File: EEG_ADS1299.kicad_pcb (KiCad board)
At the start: 2 copper layers, 45.2 x 21.7 mm, 70 parts, among them IC1 ADS1299, P1 CONN_2, P2 CONN_2, P3 CONN_1, P4 CONN_1, P5 CONN_01X08, U1 TPS61221, U2 TPS61222, U3 NRF528XX-QFAA, U4 MPU-9250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

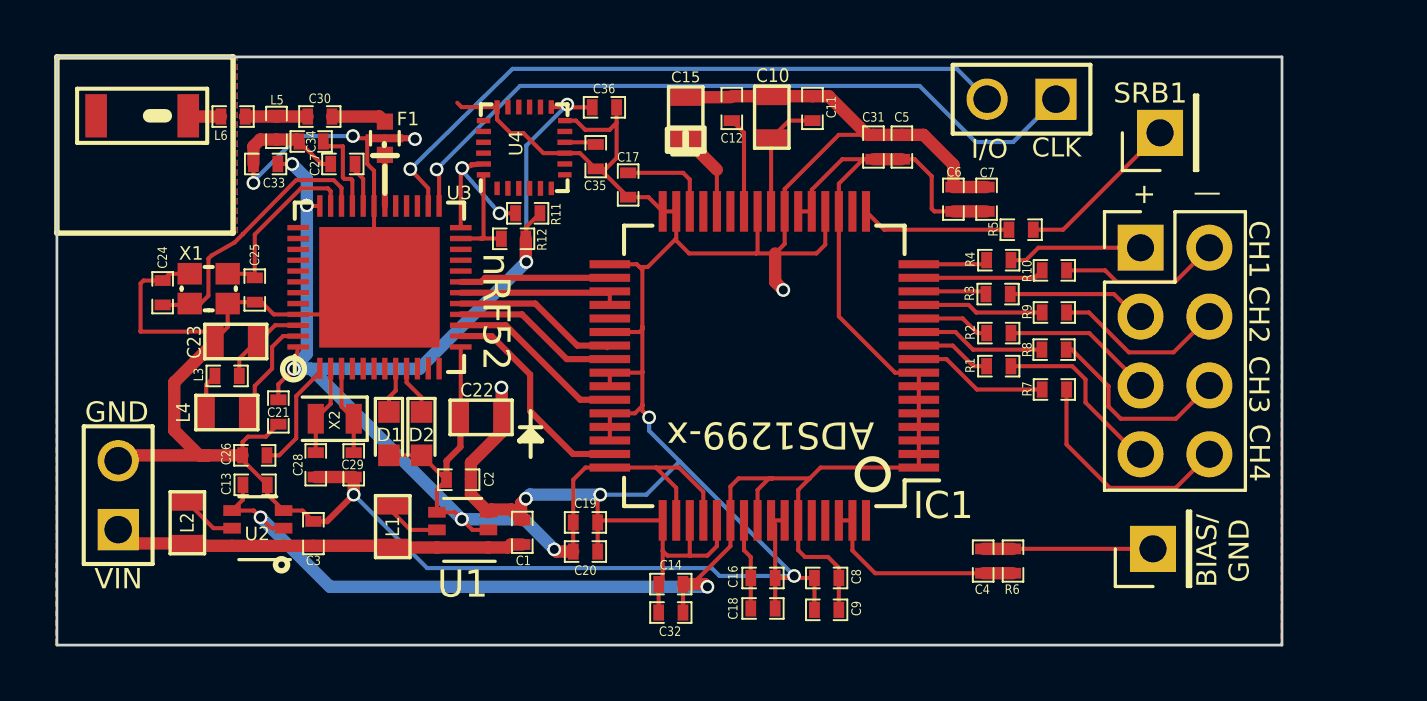
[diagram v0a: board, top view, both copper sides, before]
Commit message: Updated schematic, deleted extra pin headers. Removed extra components from pcb file.
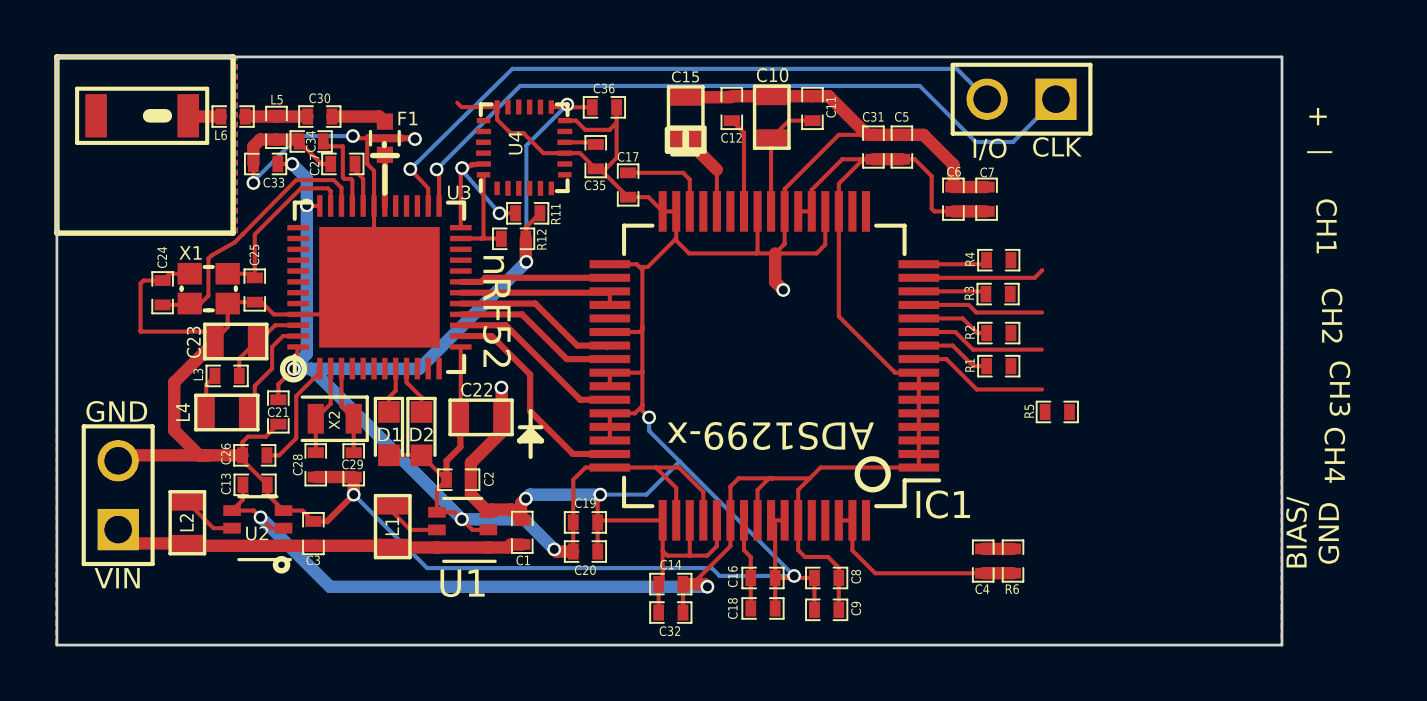
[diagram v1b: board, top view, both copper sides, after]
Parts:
- removed P3, P4: CONN_1, Pin_Headers:Pin_Header_Straight_1x01_Pitch2.54mm
- removed P5: CONN_01X08, Pin_Headers:Pin_Header_Straight_2x04_Pitch2.54mm
- removed R10, R7, R8, R9: 30k, SM0402
- moved R5 6.86 mm to (302.8, 138.6)
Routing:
- net /IN4-: track 8.48 -> 0.00 mm
- net /IN3-: track 7.46 -> 0.00 mm
- net /IN4: track 6.62 -> 0.00 mm
- net /IN2-: track 6.43 -> 0.00 mm
- net /SRB1: track 6.16 -> 0.00 mm
- net /IN1-: track 5.97 -> 0.00 mm
- net /IN3: track 5.60 -> 0.00 mm
- net Net-(IC1-Pad17): track 5.56 -> 0.00 mm
- net /IN1: track 5.23 -> 0.00 mm
- net /BIASIN: track 6.27 -> 1.10 mm
- net /IN2: track 5.15 -> 0.00 mm
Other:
- board text removed: "SRB1"

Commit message: Finished pcb draft for 4-ch with 2x INA828 (single-ended only).
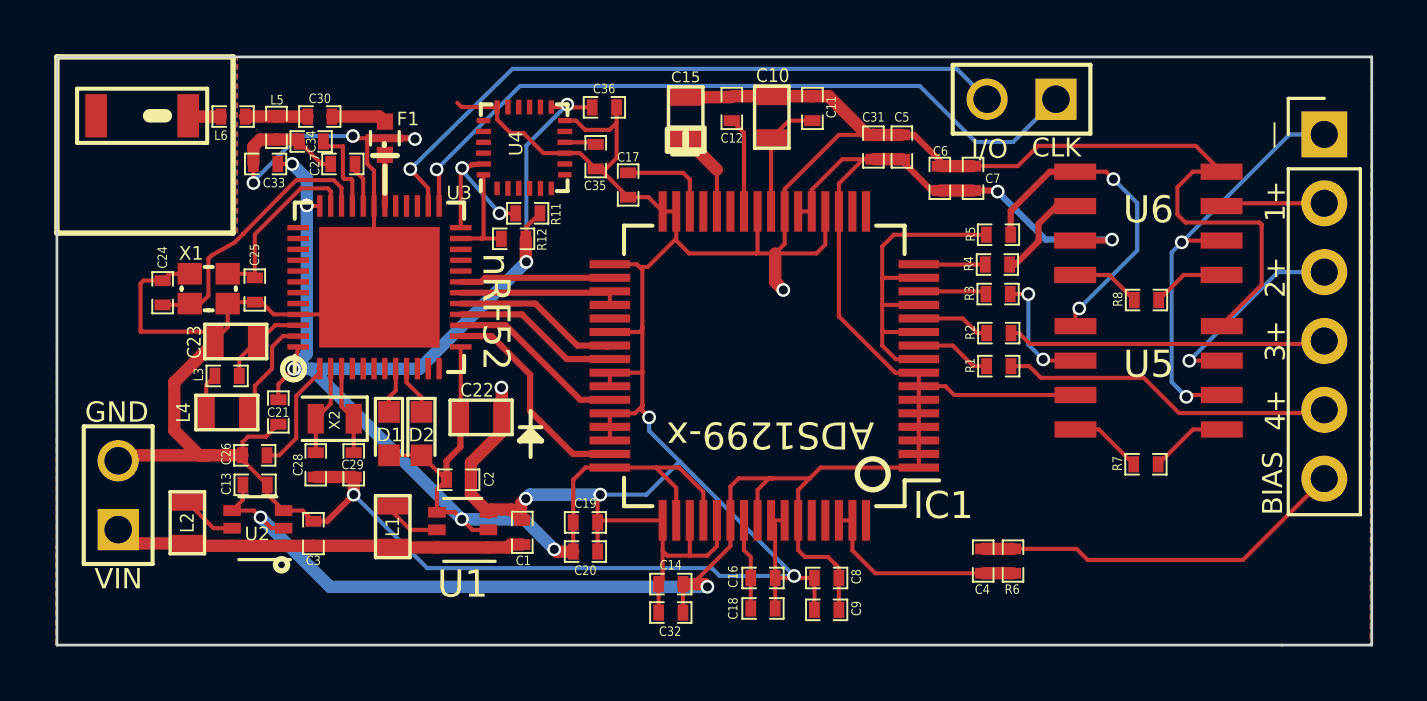
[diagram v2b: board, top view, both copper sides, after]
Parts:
- added P3: CONN_01X06, Pin_Headers:Pin_Header_Straight_1x06_Pitch2.54mm, F.Cu at (312.7, 128.4)
- added R7: 10k, SM0402, F.Cu at (306.1, 140.5)
- added R8: 10k, SM0402, F.Cu at (306.1, 134.5)
- added U5: INA828, INA828:SOIC_8_4.9mm_x_3.91, F.Cu at (306.2, 137.3)
- added U6: INA828, INA828:SOIC_8_4.9mm_x_3.91, F.Cu at (306.2, 131.6)
- moved R5 6.89 mm to (300.6, 132.1)
- moved C6 0.92 mm to (298.5, 130.0)
- moved C7 0.92 mm to (299.7, 130.0)
- moved R4 0.17 mm to (300.6, 133.2)
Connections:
- IC1 pad 11: Net-(IC1-Pad11) -> /IN1-
- IC1 pad 13: Net-(IC1-Pad13) -> /IN1-
- IC1 pad 15: Net-(IC1-Pad15) -> /IN1-
- IC1 pad 9: Net-(IC1-Pad9) -> /IN1-
- R3 pad 2: /IN2 -> Net-(R3-Pad2)
- R4 pad 2: /IN1 -> Net-(R4-Pad2)
- R5 pad 1: Net-(IC1-Pad17) -> /IN1-
- R5 pad 2: /SRB1 -> /INN-
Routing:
- net AVSS: track 184.3 -> 203.5 mm
- net /NEG_INPUT: track 0.00 -> 15.8 mm, vias 0 -> 2
- net /IN1-: track 0.00 -> 13.5 mm
- net /BIASIN: track 1.10 -> 14.0 mm
- net /IN4: track 0.00 -> 12.3 mm
- net /IN3: track 0.00 -> 12.2 mm
- net /INN-: track 0.00 -> 12.1 mm, vias 0 -> 2
- net AVDD: track 66.2 -> 78.2 mm, vias 2 -> 4
- net /IN2: track 0.00 -> 7.54 mm, vias 0 -> 1
- net Net-(IC1-Pad9): track 5.01 -> 0.00 mm
- net Net-(IC1-Pad11): track 4.88 -> 0.00 mm
- net Net-(IC1-Pad13): track 4.67 -> 0.00 mm
- net Net-(IC1-Pad15): track 4.66 -> 0.00 mm
- net Net-(R3-Pad2): track 0.00 -> 4.51 mm, vias 0 -> 2
- net /IN1: track 0.00 -> 3.83 mm
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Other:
- board size 45.2 x 21.7 mm -> 48.5 x 21.7 mm
- board text added: "1+"
- board text added: "2+"
- board text added: "3+"
- board text added: "4+"
- board text added: "BIAS"
- board text removed: "+"
- board text removed: "BIAS/ GND"
- board text removed: "CH1"
- board text removed: "CH2"
- board text removed: "CH3"
- board text removed: "CH4"
